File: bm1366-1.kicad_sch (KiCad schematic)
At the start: 63 parts, among them U1 25MHz, U13 ADP171AUJ-R7, U14 BM1366_mode1, U23 ADP171AUJ-R7

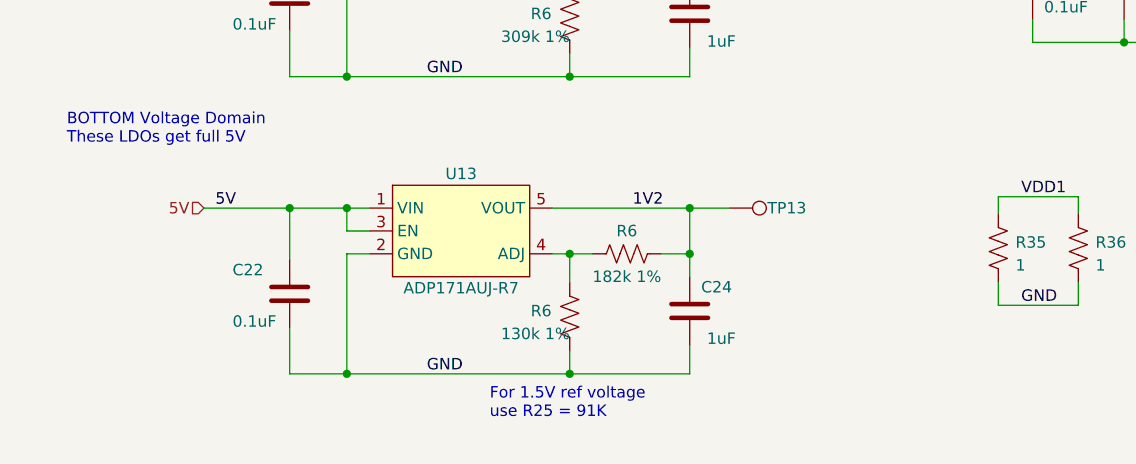
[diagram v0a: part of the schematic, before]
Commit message: add note to specify resistor value for 1.8V reference voltage
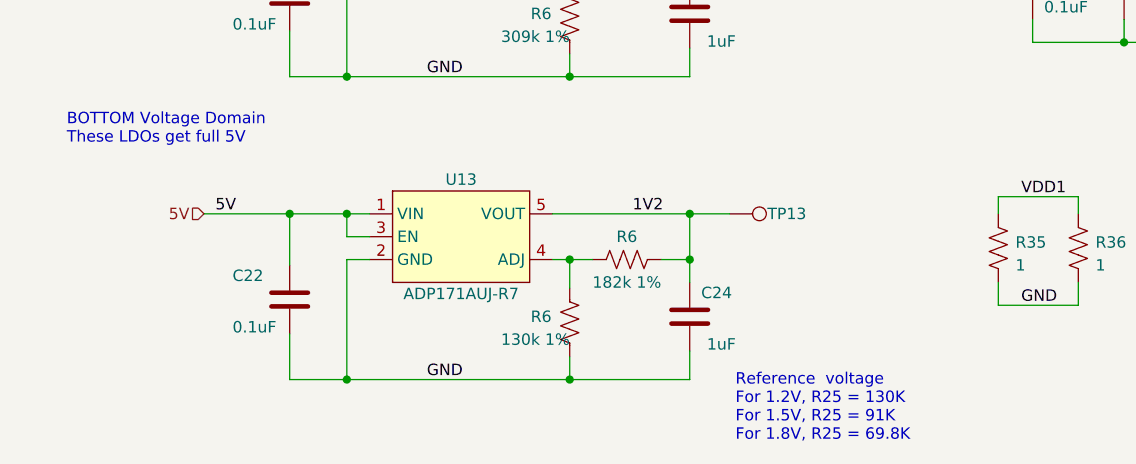
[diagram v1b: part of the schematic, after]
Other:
- note added: "Reference voltage For 1.2V, R25 = 130K For 1.5V, R25 = 91K For 1.8V, R25 = 69.8K"
- note removed: "For 1.5V ref voltage use R25 = 91K"
- moved on the sheet: C22, C24, R6, TP13, U13

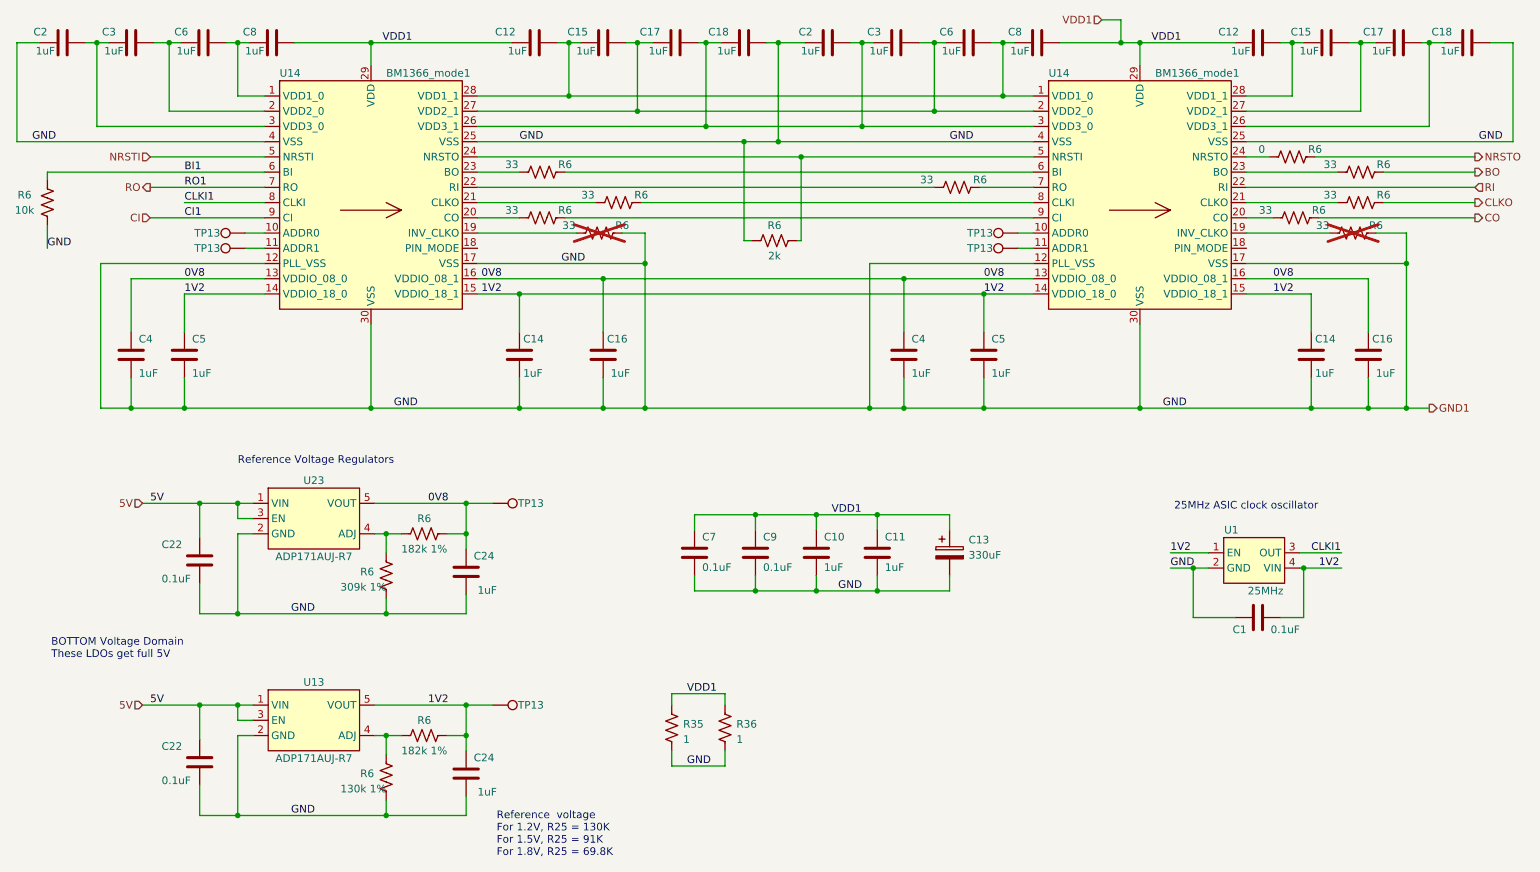
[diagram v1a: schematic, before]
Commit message: updated 1V2 to 1V8 and updated the BOM
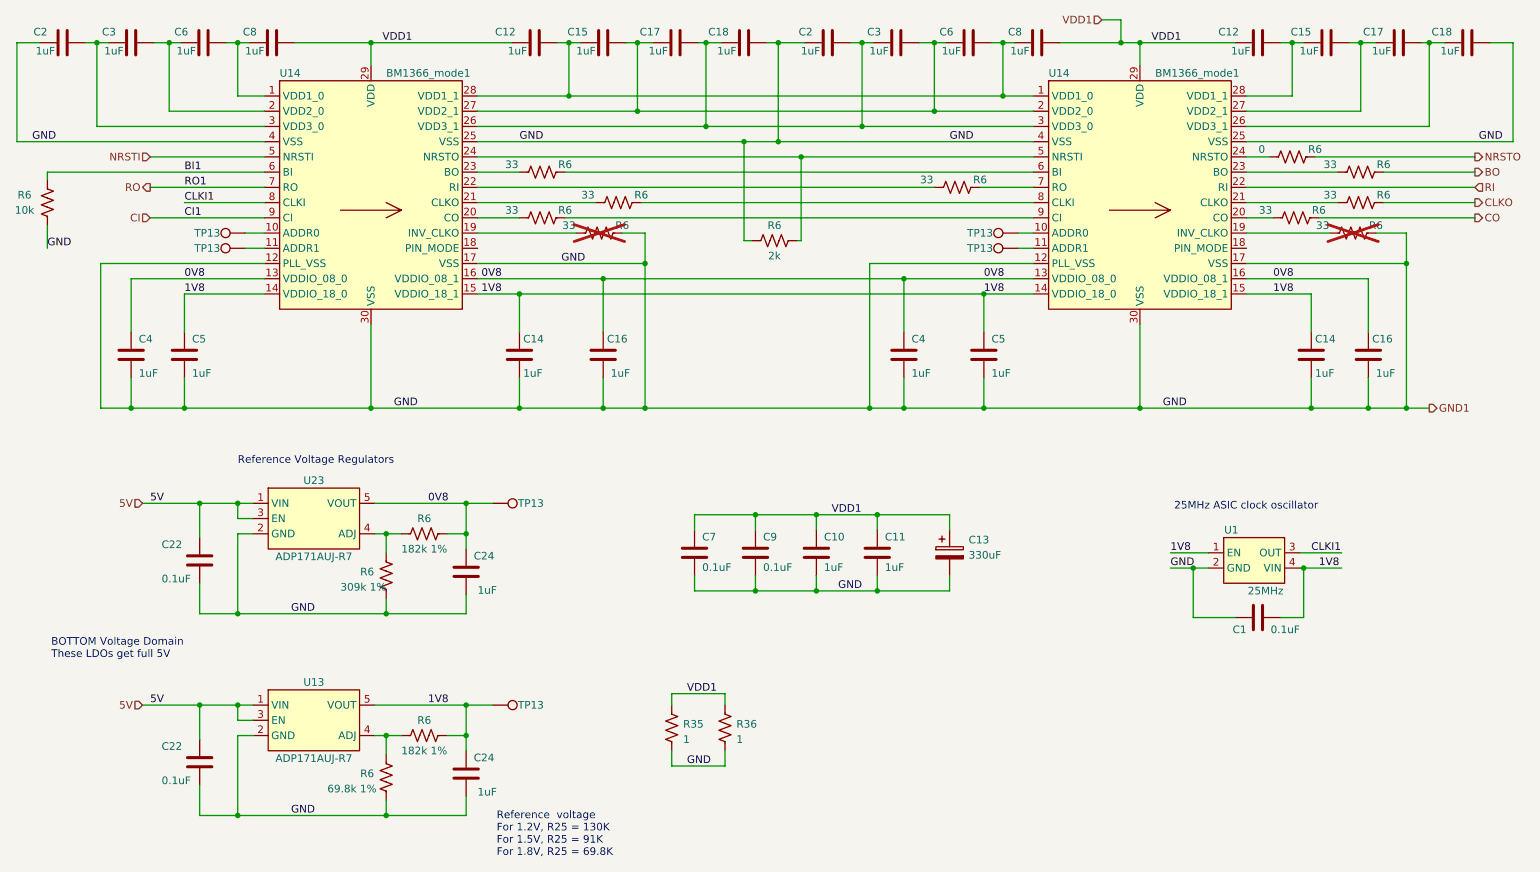
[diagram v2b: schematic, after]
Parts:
- R6: value 130k 1% -> 69.8k 1%; DK YAG2969CT-ND -> YAG3216CT-ND; PARTNO RC0402FR-07130KL -> RC0402FR-0769K8L
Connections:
- net 1V2 renamed 1V8
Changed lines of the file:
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@@
     (effects (font (size 1.27 1.27)) (justify left bottom))
   )
-  (label "1V2" (at 205.74 151.13 0) (fields_autoplaced)
+  (label "1V8" (at 205.74 151.13 0) (fields_autoplaced)
     (effects (font (size 1.27 1.27)) (justify left bottom))
   )
@@
     (effects (font (size 1.27 1.27)) (justify left bottom))
   )
-  (label "1V2" (at 90.805 107.95 0) (fields_autoplaced)
-    (effects (font (size 1.27 1.27)) (justify left bottom))
-  )
-  (label "1V2" (at 230.505 153.67 0) (fields_autoplaced)
+  (label "1V8" (at 90.805 107.95 0) (fields_autoplaced)
+    (effects (font (size 1.27 1.27)) (justify left bottom))
+  )
+  (label "1V8" (at 230.505 153.67 0) (fields_autoplaced)
     (effects (font (size 1.27 1.27)) (justify left bottom))
   )
@@
     (effects (font (size 1.27 1.27)) (justify left bottom))
   )
-  (label "1V2" (at 81.915 176.53 0) (fields_autoplaced)
+  (label "1V8" (at 81.915 176.53 0) (fields_autoplaced)
     (effects (font (size 1.27 1.27)) (justify left bottom))
   )
@@
     (effects (font (size 1.27 1.27)) (justify left bottom))
   )
-  (label "1V2" (at 41.275 107.95 0) (fields_autoplaced)
-    (effects (font (size 1.27 1.27)) (justify left bottom))
-  )
-  (label "1V2" (at 174.625 107.95 0) (fields_autoplaced)
+  (label "1V8" (at 41.275 107.95 0) (fields_autoplaced)
+    (effects (font (size 1.27 1.27)) (justify left bottom))
+  )
+  (label "1V8" (at 174.625 107.95 0) (fields_autoplaced)
     (effects (font (size 1.27 1.27)) (justify left bottom))
   )
@@
     (effects (font (size 1.27 1.27)) (justify left bottom))
   )
-  (label "1V2" (at 222.885 107.95 0) (fields_autoplaced)
+  (label "1V8" (at 222.885 107.95 0) (fields_autoplaced)
     (effects (font (size 1.27 1.27)) (justify left bottom))
   )
@@
       (effects (font (size 1.27 1.27)))
     )
-    (property "Value" "130k 1%" (at 71.12 190.5 0)
+    (property "Value" "69.8k 1%" (at 69.215 190.5 0)
       (effects (font (size 1.27 1.27)))
     )
@@
       (effects (font (size 1.27 1.27)) hide)
     )
-    (property "DK" "YAG2969CT-ND" (at 74.93 188.595 0)
-      (effects (font (size 1.27 1.27)) hide)
-    )
-    (property "PARTNO" "RC0402FR-07130KL" (at 74.93 188.595 0)
-      (effects (font (size 1.27 1.27)) hide)
-    )
+    (property "DK" "YAG3216CT-ND" (at 74.93 188.595 0)
+      (effects (font (size 1.27 1.27)) hide)
+    )
+    (property "PARTNO" "RC0402FR-0769K8L" (at 74.93 188.595 0)
+      (effects (font (size 1.27 1.27)) hide)
+    )

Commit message: change 1 ohm power resistors to 2 watt parts, changed schematic and BOM
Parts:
- R35, R36: DK 118-CR2512-F/-1R00ELFCT-ND -> CRM2512-JW-1R0ELFCT-ND; PARTNO CR2512-F/-1R00ELF -> CRM2512-JW-1R0ELF
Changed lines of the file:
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@@
       (effects (font (size 1.27 1.27)) hide)
     )
-    (property "DK" "118-CR2512-F/-1R00ELFCT-ND" (at 131.445 180.34 0)
-      (effects (font (size 1.27 1.27)) hide)
-    )
-    (property "PARTNO" "CR2512-F/-1R00ELF" (at 131.445 180.34 0)
+    (property "DK" "CRM2512-JW-1R0ELFCT-ND" (at 131.445 180.34 0)
+      (effects (font (size 1.27 1.27)) hide)
+    )
+    (property "PARTNO" "CRM2512-JW-1R0ELF" (at 131.445 180.34 0)
       (effects (font (size 1.27 1.27)) hide)
     )
@@
       (effects (font (size 1.27 1.27)) hide)
     )
-    (property "DK" "118-CR2512-F/-1R00ELFCT-ND" (at 122.555 180.34 0)
-      (effects (font (size 1.27 1.27)) hide)
-    )
-    (property "PARTNO" "CR2512-F/-1R00ELF" (at 122.555 180.34 0)
-      (effects (font (size 1.27 1.27)) hide)
-    )
+    (property "DK" "CRM2512-JW-1R0ELFCT-ND" (at 122.555 180.34 0)
+      (effects (font (size 1.27 1.27)) hide)
+    )
+    (property "PARTNO" "CRM2512-JW-1R0ELF" (at 122.555 180.34 0)
+      (effects (font (size 1.27 1.27)) hide)
+    )

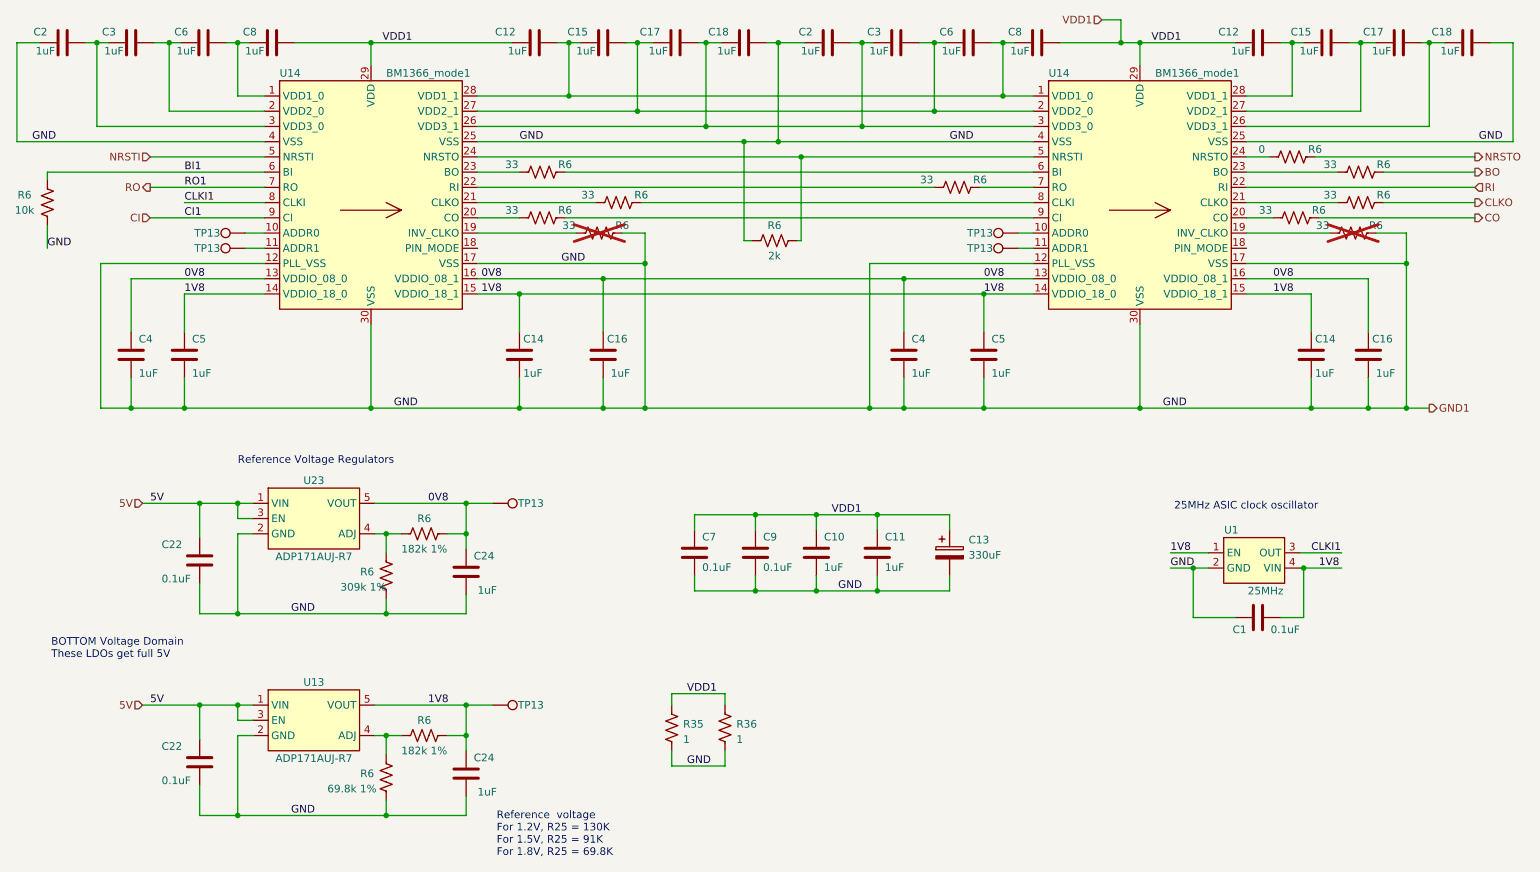
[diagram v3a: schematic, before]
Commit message: remove old 5V power supply, prepare footprints for new 5V buck supply, switch fans to 12V
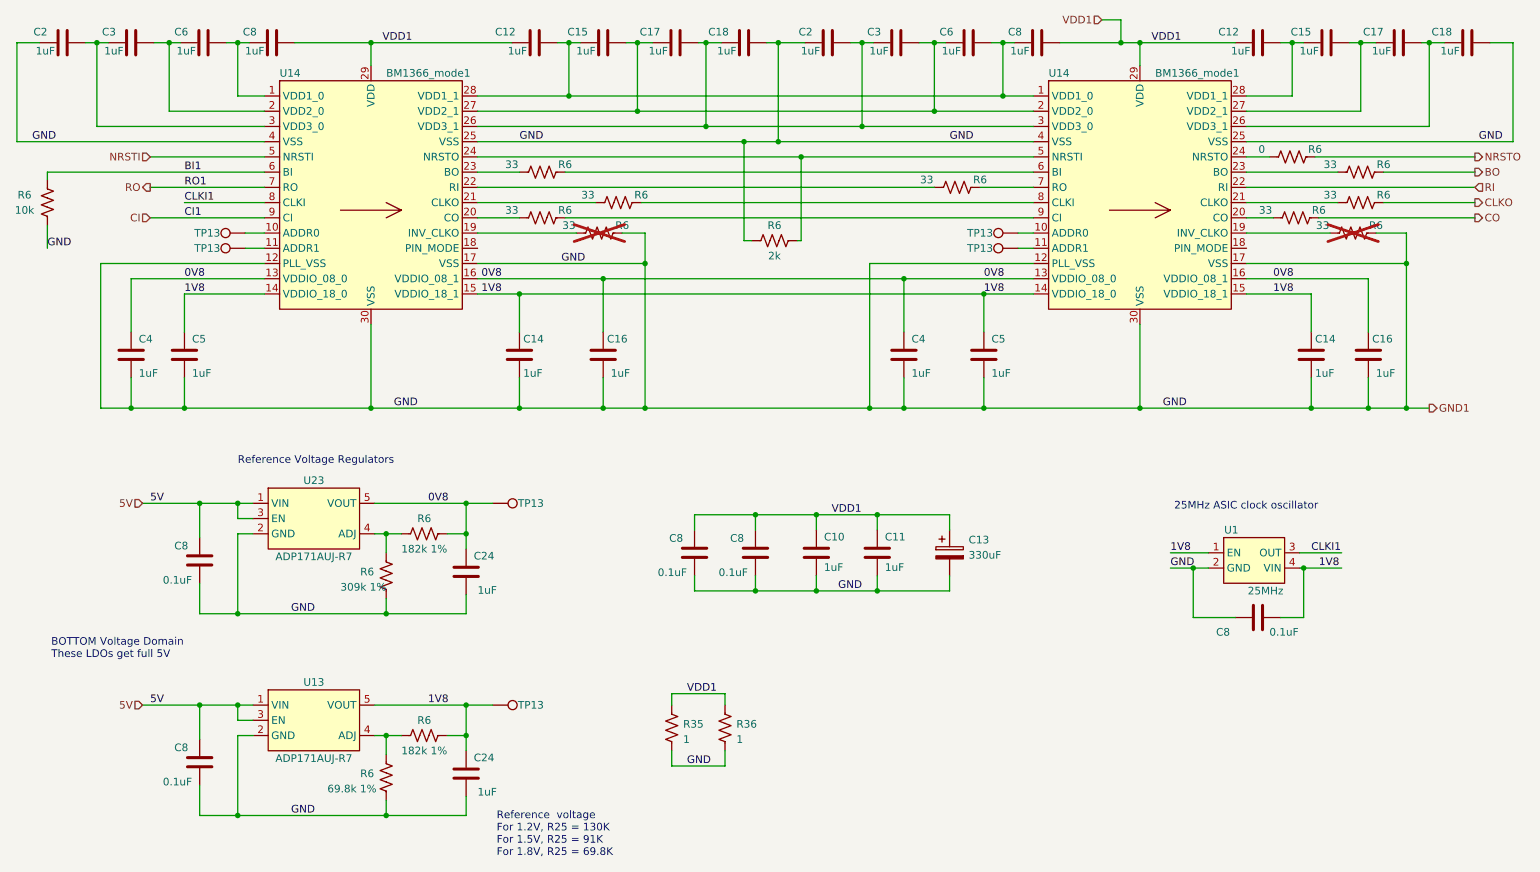
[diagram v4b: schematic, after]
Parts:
- removed C1, C22 (x2), C7, C9: 0.1uF, Capacitor_SMD:C_0402_1005Metric, symbol Device:C
- added C8 (x5): 0.1uF, Capacitor_SMD:C_0402_1005Metric, symbol Device:C
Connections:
- net 1V8: now also C8.1
- net 5V: now also C8.2, C8.2
- net GND1: now also C8.1, C8.1, C8.1, C8.1, C8.2
- net VDD1: now also C8.2, C8.2

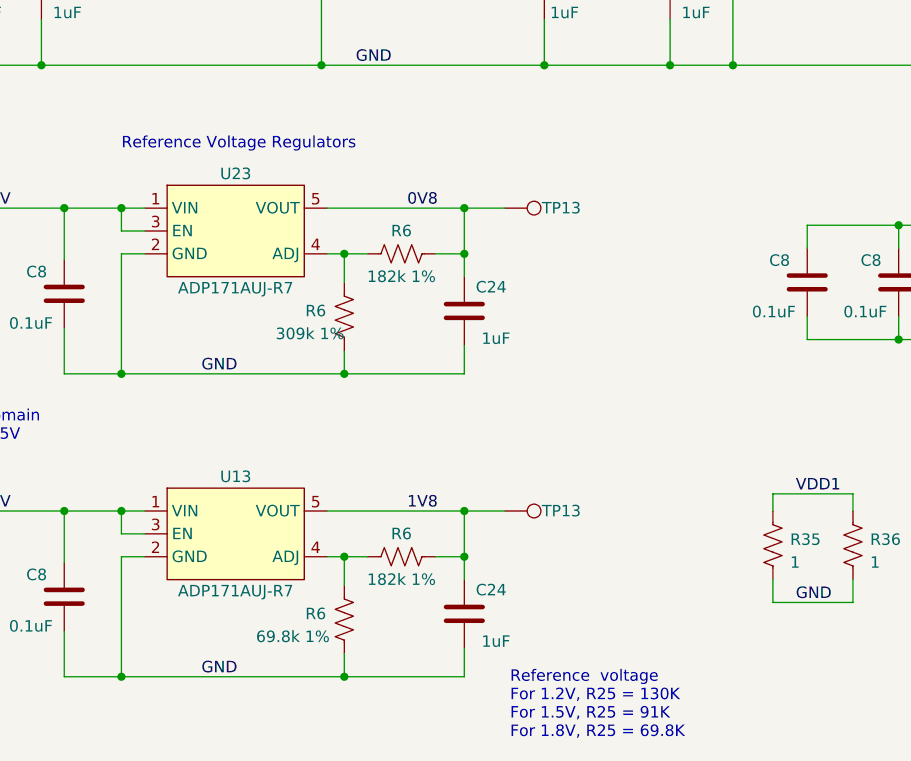
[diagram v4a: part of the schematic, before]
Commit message: switch out reference LDOs for AP7331
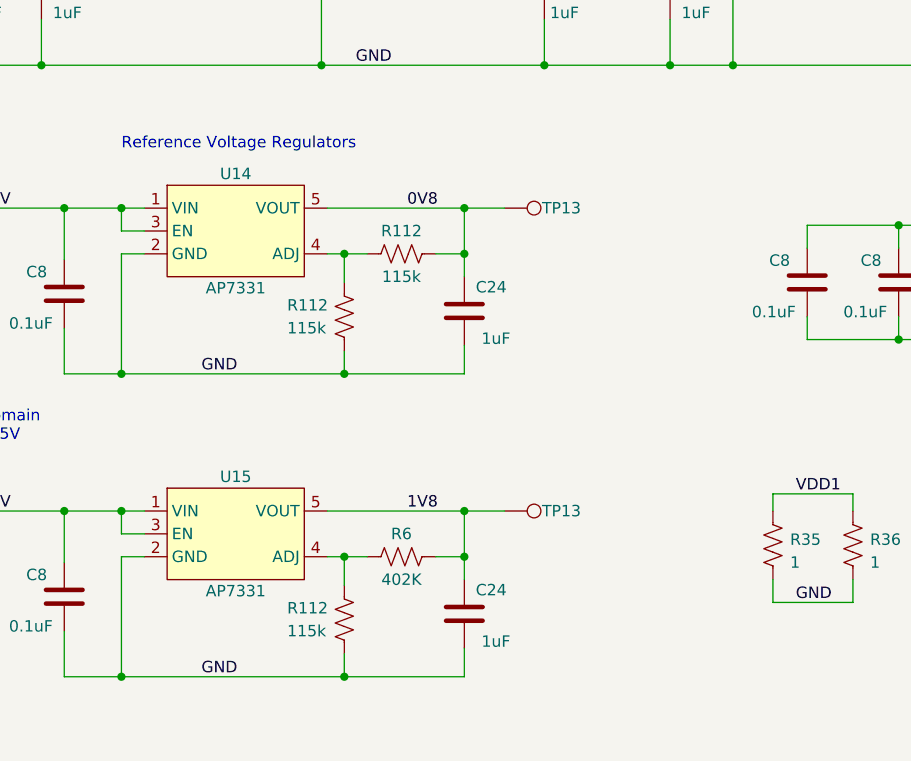
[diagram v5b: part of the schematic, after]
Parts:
- removed R6: 69.8k 1%, Resistor_SMD:R_0402_1005Metric, symbol Device:R_US
- removed R6: 182k 1%, Resistor_SMD:R_0402_1005Metric, symbol Device:R_US
- removed R6: 309k 1%, Resistor_SMD:R_0402_1005Metric, symbol Device:R_US
- removed U13, U23: ADP171AUJ-R7, Package_TO_SOT_SMD:TSOT-23-5, symbol bitaxe:ADP171AUJ-R7
- added R112 (x3): 115k, Resistor_SMD:R_0402_1005Metric, symbol Device:R_US
- added U14, U15: AP7331, Package_TO_SOT_SMD:TSOT-23-5, symbol bitaxe:AP7331
- R6: value 182k 1% -> 402K
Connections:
- net 0V8: now also R112.2, U14.5 (VOUT)
- net 1V8: now also U15.5 (VOUT)
- net 5V: now also U14.1 (VIN), U14.3 (EN), U15.1 (VIN), U15.3 (EN)
- net GND1: now also R112.1, R112.1, U14.2 (GND), U15.2 (GND)
- net at R6.2: now also R112.2, U15.4 (ADJ)
- new net: R112.1, R112.2, U14.4 (ADJ)
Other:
- note removed: "Reference voltage For 1.2V, R25 = 130K For 1.5V, R25 = 91K For 1.8V, R25 = 69.8K"

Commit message: Fix DK partnumber for 402K resistor
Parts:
- R6: DK YAG3015CT-ND -> YAG3151CT-ND; PARTNO RC0402FR-07182KL -> RC0402FR-07402KL
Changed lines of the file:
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@@
       (effects (font (size 1.27 1.27)) hide)
     )
-    (property "DK" "YAG3015CT-ND" (at 81.28 181.61 0)
+    (property "DK" "YAG3151CT-ND" (at 81.28 181.61 0)
       (effects (font (size 1.27 1.27)) hide)
     )
-    (property "PARTNO" "RC0402FR-07182KL" (at 81.28 181.61 0)
+    (property "PARTNO" "RC0402FR-07402KL" (at 81.28 181.61 0)
       (effects (font (size 1.27 1.27)) hide)
     )

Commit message: re-annotate all components
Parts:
- renumbered U14 to U10, U15 to U11
